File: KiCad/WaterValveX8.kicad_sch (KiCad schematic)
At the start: 50 parts, among them J1 Conn_01x04_Male, J2 Barrel_Jack, J3 Conn_01x03_Male, J4 Conn_01x01_Male, J5 Conn_01x04_Male, J6 Screw_Terminal_01x03, J7 Screw_Terminal_01x03, J8 Screw_Terminal_01x03, J9 Screw_Terminal_01x02, Q1 IRLML2502, Q2 IRLML2502, Q3 IRLML2502, Q4 IRLML2502, U1 Project_DCDC_01, U2 SeedStudio XIAO ESP32 C3 v1, U3 L7805

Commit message: First X8 layout
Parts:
- removed J1: Conn_01x04_Male, Connector_PinHeader_2.54mm:PinHeader_1x04_P2.54mm_Vertical, symbol Connector:Conn_01x04_Male
- removed J2: Barrel_Jack, LOCAL1:BarrelJack1, symbol LOCAL1:BarrelJack1
- removed U1: Project_DCDC_01, LOCAL1:DCDC_01, symbol LOCAL1:DCDC_01
- removed U2: SeedStudio XIAO ESP32 C3 v1, LOCAL1:XIAO_ESP32C3_THT, symbol LOCAL1:XIAO_ESP32C3_THT
- added D13, D20, D23, D26, D29: LED, LED_SMD:LED_0805_2012Metric_Pad1.15x1.40mm_HandSolder, symbol Device:LED
- added D14, D15, D16, D17, D18, D19, D22, D25, D28: LED, LED_THT:LED_D3.0mm, symbol Device:LED
- added D21, D24, D27, D30: 1N4148, Diode_SMD:D_MiniMELF, symbol Device:D
- added J10, J2: Screw_Terminal_01x03, TerminalBlock_Phoenix:TerminalBlock_Phoenix_PT-1,5-3-3.5-H_1x03_P3.50mm_Horizontal, symbol Connector:Screw_Terminal_01x03
- added J11: Conn_01x03_Pin, Connector_PinHeader_2.54mm:PinHeader_1x03_P2.54mm_Vertical, symbol Connector:Conn_01x03_Pin
- added Q5, Q6, Q7, Q8: IRLML2502, Package_TO_SOT_SMD:SOT-23_Handsoldering, symbol Transistor_FET:IRLML6244
- added R14, R17, R18, R19, R20, R21, R22, R23: 1k, Resistor_SMD:R_0805_2012Metric_Pad1.20x1.40mm_HandSolder, symbol Device:R
- added U2: XIAO-ESP32-C6-SMD, LOCAL1:XIAO-ESP32-C6-SMD, symbol LOCAL1:XIAO-ESP32-C6-SMD
- C1, C3: footprint Capacitor_Tantalum_SMD:CP_EIA-3216-18_Kemet-A_Pad1.58x1.35mm_HandSolder -> Capacitor_SMD:C_1206_3216Metric_Pad1.33x1.80mm_HandSolder
- D11: footprint LED_SMD:LED_0805_2012Metric_Pad1.15x1.40mm_HandSolder -> LED_THT:LED_D3.0mm
- D12, D4, D6, D9: value 1N4007 -> 1N4148; footprint Diode_THT:D_DO-41_SOD81_P3.81mm_Vertical_KathodeUp -> Diode_SMD:D_MiniMELF
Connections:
- net +3V3: now also D13.2 (A), D14.2 (A), U2.3 (GPIO2_A2_D2)
- net +5V: now also U2.1 (GPIO0_A0_D0)
- net +VSW: now also D15.2 (A), D16.2 (A), D17.2 (A), D18.2 (A), D19.2 (A), D20.2 (A), D21.1 (K), D22.2 (A), D23.2 (A), D24.1 (K), D25.2 (A), D26.2 (A), D27.1 (K), D28.2 (A), D29.2 (A), D30.1 (K), J2.1 (Pin_1)
- net GND: now also J10.3 (Pin_3), J11.3 (Pin_3), Q5.2 (S), Q6.2 (S), Q7.2 (S), Q8.2 (S), U2.2 (GPIO1_A1_D1), U2.20 (GND)
- net GPIO2: now also U2.14 (5V)
- net RX: now also J11.1 (Pin_1), R22.1, U2.7 (GPIO16_D6_TX)
- net SCL: now also R18.1, U2.9 (GPIO19_D8_SCK)
- net SDA: now also R14.1, U2.10 (GPIO20_D9_MISO)
- net TX: now also J11.2 (Pin_2), R20.1, U2.8 (GPIO17_D7_RX)
- net at D1.1 (K): now also U2.5 (GPIO22_D4_SDA)
- net at D3.1 (K), R7.2: now also D15.1 (K)
- net at D5.1 (K), R10.2: now also D16.1 (K)
- net at D8.1 (K), R13.2: now also D17.1 (K)
- net at D10.1 (K), R15.2: now also D18.1 (K)
- net at D11.1 (K), R16.2: now also D13.1 (K)
- net at D1.2 (A), R1.1: now also D14.1 (K)
- net GPIO10 renamed D10
- net D10: now also U2.4 (GPIO21_D3)
- net GPIO3 renamed D1
- net D1: now also U2.13 (GND)
- net GPIO4 renamed D2
- net D2: now also U2.12 (3V3)
- net GPIO5 renamed D3
- net D3: now also U2.11 (GPIO18_D10_MOSI)
- net GPIO8 renamed D8
- net D8: now also U2.6 (GPIO23_D5_SCL)
- new net: D28.1 (K), D29.1 (K), R23.2
- new net: D19.1 (K), D20.1 (K), R17.2
- new net: Q6.1 (G), R18.2
- new net: D25.1 (K), D26.1 (K), R21.2
- new net: Q7.1 (G), R20.2
- new net: Q5.1 (G), R14.2
- new net: D22.1 (K), D23.1 (K), R19.2
- new net: Q8.1 (G), R22.2
- new net Relay5: D21.2 (A), J10.2 (Pin_2), Q5.3 (D), R17.1
- new net Relay6: D24.2 (A), J10.1 (Pin_1), Q6.3 (D), R19.1
- new net Relay7: D27.2 (A), J2.3 (Pin_3), Q7.3 (D), R21.1
- new net Relay8: D30.2 (A), J2.2 (Pin_2), Q8.3 (D), R23.1
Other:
- note added: "D1 - Valve 1 D2 - Valve 2 D3 - Valve 3 D8 - Valve 4 D9 - LED D10 - Water meter 2 - 8 - 9 - - H normal 1 NA 1 SPI boot 1 1 0 Download"
- note removed: "IO1 - Valve 1 IO2 - Valve 2 IO3 - Valve 3 IO8 - Valve 4 IO9 - LED IO10 - Water meter 2 - 8 - 9 - - H normal 1 NA 1 SPI boot (default) Flash boot 1 1 0 Download"
- moved on the sheet: C1, C2, C3, D10, D12, D3, D4, D5, D6, D8, D9, H5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

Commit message: Diode footprint changes
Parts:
- D12, D21, D24, D27, D30, D4, D6, D7, D9: footprint Diode_SMD:D_MiniMELF -> Diode_SMD:D_SOD-123
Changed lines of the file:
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@@
 			)
 		)
-		(property "Footprint" "Diode_SMD:D_MiniMELF"
+		(property "Footprint" "Diode_SMD:D_SOD-123"
 			(at 167.64 105.41 0)
 			(effects
@@
 			)
 		)
-		(property "Footprint" "Diode_SMD:D_MiniMELF"
+		(property "Footprint" "Diode_SMD:D_SOD-123"
 			(at 179.07 105.41 0)
 			(effects
@@
 			)
 		)
-		(property "Footprint" "Diode_SMD:D_MiniMELF"
+		(property "Footprint" "Diode_SMD:D_SOD-123"
 			(at 190.5 105.41 0)
 			(effects
@@
 			)
 		)
-		(property "Footprint" "Diode_SMD:D_MiniMELF"
+		(property "Footprint" "Diode_SMD:D_SOD-123"
 			(at 201.93 105.41 0)
 			(effects
@@
 			)
 		)
-		(property "Footprint" "Diode_SMD:D_MiniMELF"
+		(property "Footprint" "Diode_SMD:D_SOD-123"
 			(at 62.23 47.625 0)
 			(effects
@@
 			)
 		)
-		(property "Footprint" "Diode_SMD:D_MiniMELF"
+		(property "Footprint" "Diode_SMD:D_SOD-123"
 			(at 213.36 40.64 0)
 			(effects
@@
 			)
 		)
-		(property "Footprint" "Diode_SMD:D_MiniMELF"
+		(property "Footprint" "Diode_SMD:D_SOD-123"
 			(at 224.79 40.64 0)
 			(effects
@@
 			)
 		)
-		(property "Footprint" "Diode_SMD:D_MiniMELF"
+		(property "Footprint" "Diode_SMD:D_SOD-123"
 			(at 201.93 40.64 0)
 			(effects
@@
 			)
 		)
-		(property "Footprint" "Diode_SMD:D_MiniMELF"
+		(property "Footprint" "Diode_SMD:D_SOD-123"
 			(at 236.22 40.64 0)
 			(effects

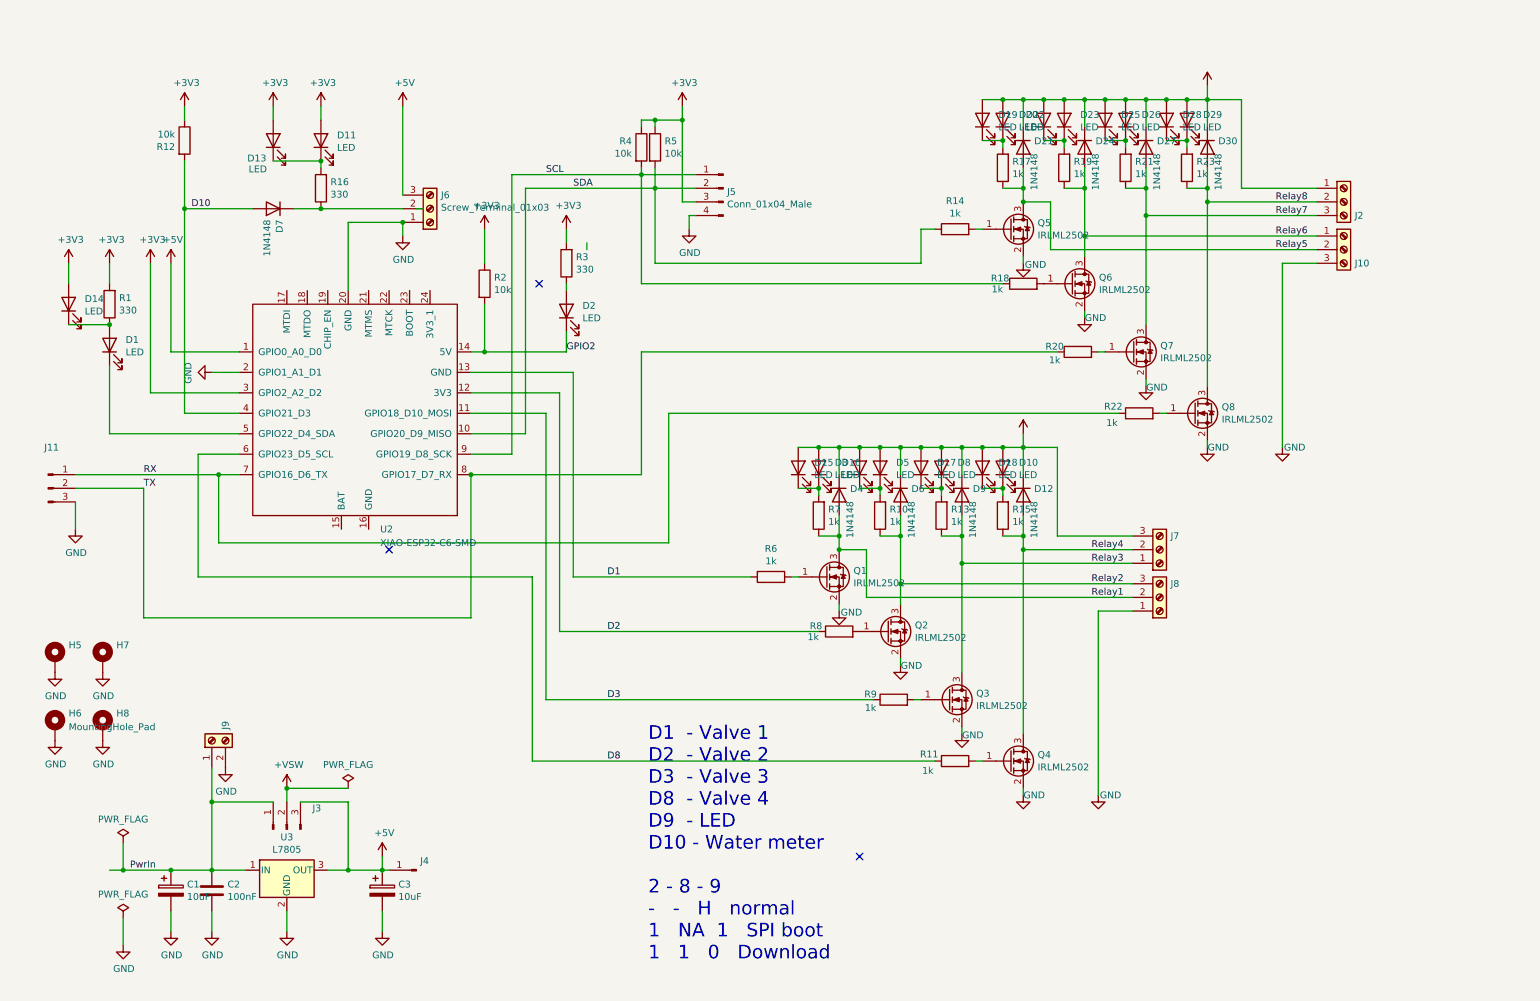
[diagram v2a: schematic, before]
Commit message: Changed to combined C3/C6 and step-down PSU
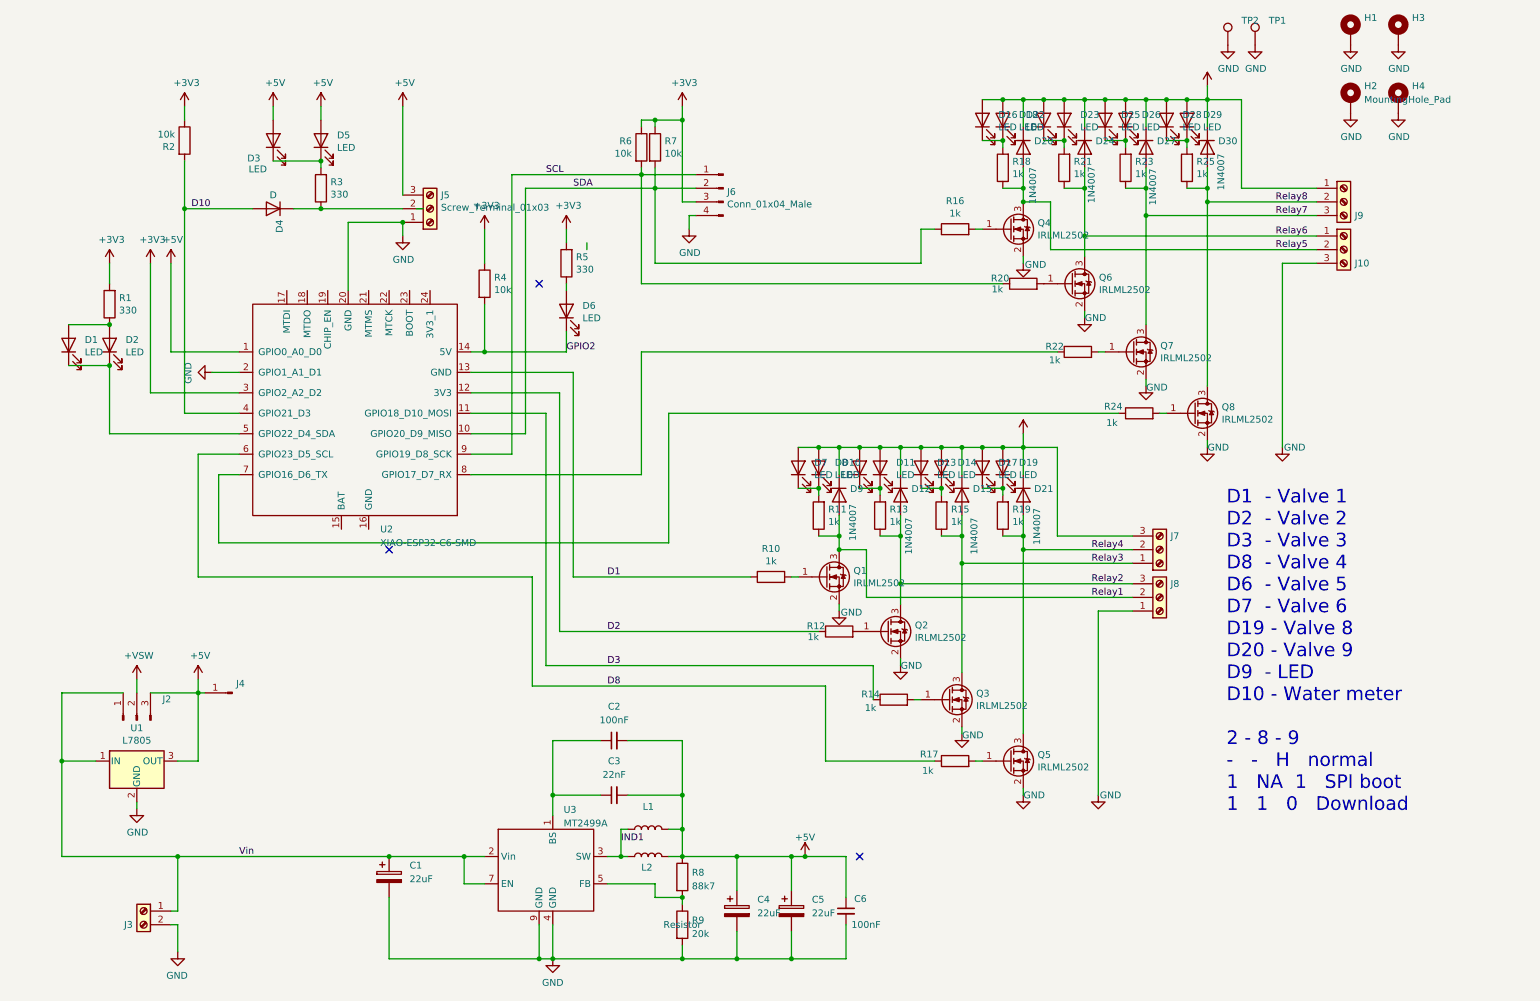
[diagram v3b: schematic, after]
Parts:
- removed C1, C3: 10uF, Capacitor_SMD:C_1206_3216Metric_Pad1.33x1.80mm_HandSolder, symbol Device:CP
- removed C2: 100nF, Capacitor_SMD:C_0805_2012Metric_Pad1.18x1.45mm_HandSolder, symbol Device:C
- removed J11: Conn_01x03_Pin, Connector_PinHeader_2.54mm:PinHeader_1x03_P2.54mm_Vertical, symbol Connector:Conn_01x03_Pin
- added C1, C4, C5: 22uF, Capacitor_SMD:C_1206_3216Metric_Pad1.33x1.80mm_HandSolder, symbol Device:C_Polarized
- added C2, C6: 100nF, Capacitor_SMD:C_0805_2012Metric_Pad1.18x1.45mm_HandSolder, symbol Device:C_Small
- added C3: 22nF, Capacitor_SMD:C_0805_2012Metric_Pad1.18x1.45mm_HandSolder, symbol Device:C_Small
- added L1: L, Inductor_SMD:L_Bourns-SRU8028_8.0x8.0mm, symbol Device:L
- added L2: L, Inductor_SMD:L_2512_6332Metric_Pad1.52x3.35mm_HandSolder, symbol Device:L
- added R8: 88k7, Resistor_SMD:R_0805_2012Metric_Pad1.20x1.40mm_HandSolder, symbol Device:R
- added R9: 20k, Resistor_SMD:R_0805_2012Metric_Pad1.20x1.40mm_HandSolder, symbol Device:R
- added TP1, TP2: TestPoint, TestPoint:TestPoint_THTPad_1.0x1.0mm_Drill0.5mm, symbol Connector:TestPoint
- added U3: MT2499A, Package_SO:TI_SO-PowerPAD-8, symbol custom_kicad_lib_sk:MT499A
- D12: renamed from D6; value 1N4148 -> 1N4007; footprint Diode_SMD:D_SOD-123 -> Diode_SMD:D_SOD-323_HandSoldering
- D15: renamed from D9; value 1N4148 -> 1N4007; footprint Diode_SMD:D_SOD-123 -> Diode_SMD:D_SOD-323_HandSoldering
- D20: renamed from D21; value 1N4148 -> 1N4007; footprint Diode_SMD:D_SOD-123 -> Diode_SMD:D_SOD-323_HandSoldering
- D21: renamed from D12; value 1N4148 -> 1N4007; footprint Diode_SMD:D_SOD-123 -> Diode_SMD:D_SOD-323_HandSoldering
- D24, D27, D30: value 1N4148 -> 1N4007; footprint Diode_SMD:D_SOD-123 -> Diode_SMD:D_SOD-323_HandSoldering
- D4: renamed from D7; value 1N4148 -> D; footprint Diode_SMD:D_SOD-123 -> Diode_SMD:D_SOD-323_HandSoldering; symbol Diode:1N4148 -> Device:D
- D9: renamed from D4; value 1N4148 -> 1N4007; footprint Diode_SMD:D_SOD-123 -> Diode_SMD:D_SOD-323_HandSoldering
- U2: footprint LOCAL1:XIAO-ESP32-C6-SMD -> LOCAL1:XIAO-ESP32-C3C6-SMD
- renumbered D14 to D1, D16 to D10, D5 to D11, D17 to D13, D8 to D14, D19 to D16, D18 to D17, D20 to D18, D10 to D19, D1 to D2, D13 to D3, D11 to D5, D2 to D6, D15 to D7, D3 to D8, H5 to H1, H6 to H2, H7 to H3, H8 to H4, J3 to J2, J9 to J3, J6 to J5, J5 to J6, J2 to J9, Q5 to Q4, Q4 to Q5, R6 to R10, R7 to R11, R8 to R12, R10 to R13, R9 to R14, R13 to R15, R14 to R16, R11 to R17, R17 to R18, R15 to R19, R12 to R2, R18 to R20, R19 to R21, R20 to R22, R21 to R23, R22 to R24, R23 to R25, R16 to R3, R2 to R4, R3 to R5, R4 to R6, R5 to R7, U3 to U1
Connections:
- net +3V3: no longer D1.2 (A), D3.2 (A), D5.2 (A)
- net +5V: now also D3.2 (A), D5.2 (A), C2.2, C3.2, C4.1, C5.1, C6.1, L1.2, L2.2, R8.1
- net GND: now also C1.2, C4.2, C5.2, C6.2, R9.2, TP1.1, TP2.1, U3.4 (GND), U3.9 (GND)
- net at D2.1 (K), U2.5 (GPIO22_D4_SDA): now also D1.1 (K)
- net at D2.2 (A), R1.1: now also D1.2 (A); no longer D1.1 (K)
- net PwrIn renamed Vin
- net Vin: now also C1.1, U3.2 (Vin), U3.7 (EN)
- net RX: no longer names the net of R24.1, U2.7 (GPIO16_D6_TX)
- net TX: no longer names the net of R22.1, U2.8 (GPIO17_D7_RX)
- new net: C2.1, C3.1, U3.1 (BS)
- new net: R8.2, R9.1, U3.5 (FB)
- new net IND1: L1.1, L2.1, U3.3 (SW)
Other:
- note added: "D1 - Valve 1 D2 - Valve 2 D3 - Valve 3 D8 - Valve 4 D6 - Valve 5 D7 - Valve 6 D19 - Valve 8 D20 - Valve 9 D9 - LED D10 - Water meter 2 - 8 - 9 - - H normal 1 NA 1 SPI boot 1 1 0 Download"
- note removed: "D1 - Valve 1 D2 - Valve 2 D3 - Valve 3 D8 - Valve 4 D9 - LED D10 - Water meter 2 - 8 - 9 - - H normal 1 NA 1 SPI boot 1 1 0 Download"
- moved on the sheet: D1, H1, H2, H3, H4, J2, J3, J4, U1

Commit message: Title is 8x - not 4
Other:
- title: 4x Water Valve Control with Water Meter Input -> 8x Water Valve Control with Water Meter Input
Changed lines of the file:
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@@
 	(paper "A4")
 	(title_block
-		(title "4x Water Valve Control with Water Meter Input")
+		(title "8x Water Valve Control with Water Meter Input")
 		(date "2025-10-27")
 		(rev "4.0.0")
